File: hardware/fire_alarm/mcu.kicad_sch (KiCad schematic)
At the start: 2 parts, among them U4 ESP32-WROOM-32

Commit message: feat: update power mcu
Signed-off-by: Trung Hieu Nguyen <hieu.nguyenarc03@gmail.com>
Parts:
- added C8: 10uF 25V, Capacitor_SMD:C_0603_1608Metric_Pad1.08x0.95mm_HandSolder, symbol Device:C
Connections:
- net +3.3V: now also C8.2
- net GND: now also C8.1
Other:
- moved on the sheet: C9
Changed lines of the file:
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@@
 	(paper "A4")
 	(junction
-		(at 147.32 50.8)
+		(at 147.32 53.34)
 		(diameter 0)
 		(color 0 0 0 0)
 	)
-	(wire
-		(pts
-			(xy 147.32 50.8) (xy 147.32 63.5)
-		)
-		(stroke
-			(width 0)
-			(type default)
-		)
-	)
-	(wire
-		(pts
-			(xy 135.89 50.8) (xy 132.08 50.8)
-		)
-		(stroke
-			(width 0)
-			(type default)
-		)
-	)
-	(wire
-		(pts
-			(xy 147.32 50.8) (xy 143.51 50.8)
-		)
-		(stroke
-			(width 0)
-			(type default)
-		)
-	)
-	(wire
-		(pts
-			(xy 132.08 50.8) (xy 132.08 57.15)
-		)
-		(stroke
-			(width 0)
-			(type default)
-		)
-	)
-	(wire
-		(pts
-			(xy 147.32 39.37) (xy 147.32 50.8)
+	(junction
+		(at 147.32 45.72)
+		(diameter 0)
+		(color 0 0 0 0)
+	)
+	(junction
+		(at 132.08 53.34)
+		(diameter 0)
+		(color 0 0 0 0)
+	)
+	(wire
+		(pts
+			(xy 132.08 53.34) (xy 135.89 53.34)
+		)
+		(stroke
+			(width 0)
+			(type default)
+		)
+	)
+	(wire
+		(pts
+			(xy 132.08 53.34) (xy 132.08 57.15)
+		)
+		(stroke
+			(width 0)
+			(type default)
+		)
+	)
+	(wire
+		(pts
+			(xy 132.08 45.72) (xy 132.08 53.34)
+		)
+		(stroke
+			(width 0)
+			(type default)
+		)
+	)
+	(wire
+		(pts
+			(xy 147.32 45.72) (xy 147.32 53.34)
+		)
+		(stroke
+			(width 0)
+			(type default)
+		)
+	)
+	(wire
+		(pts
+			(xy 147.32 53.34) (xy 143.51 53.34)
+		)
+		(stroke
+			(width 0)
+			(type default)
+		)
+	)
+	(wire
+		(pts
+			(xy 147.32 39.37) (xy 147.32 45.72)
+		)
+		(stroke
+			(width 0)
+			(type default)
+		)
+	)
+	(wire
+		(pts
+			(xy 147.32 53.34) (xy 147.32 63.5)
 		)
 		(stroke
@@
 		(pts
 			(xy 147.32 134.62) (xy 147.32 144.78)
+		)
+		(stroke
+			(width 0)
+			(type default)
+		)
+	)
+	(wire
+		(pts
+			(xy 135.89 45.72) (xy 132.08 45.72)
+		)
+		(stroke
+			(width 0)
+			(type default)
+		)
+	)
+	(wire
+		(pts
+			(xy 143.51 45.72) (xy 147.32 45.72)
 		)
 		(stroke
@@
 	(symbol
 		(lib_id "Device:C")
-		(at 139.7 50.8 90)
+		(at 139.7 53.34 90)
 		(unit 1)
 		(exclude_from_sim no)
@@
 		(on_board yes)
 		(dnp no)
-		(fields_autoplaced yes)
 		(property "Reference" "C9"
-			(at 139.7 43.18 90)
+			(at 139.446 51.816 90)
 			(effects
 				(font
@@
 		)
 		(property "Value" "100nF 50V"
-			(at 139.7 45.72 90)
+			(at 139.446 54.356 90)
 			(effects
 				(font
@@
 		)
 		(property "Footprint" "Capacitor_SMD:C_0603_1608Metric_Pad1.08x0.95mm_HandSolder"
-			(at 143.51 49.8348 0)
+			(at 143.51 52.3748 0)
 			(effects
 				(font
@@
 		)
 		(property "Datasheet" "~"
-			(at 139.7 50.8 0)
+			(at 139.7 53.34 0)
 			(effects
 				(font
@@
 		)
 		(property "Description" "Unpolarized capacitor"
-			(at 139.7 50.8 0)
+			(at 139.7 53.34 0)
 			(effects
 				(font
@@
 					(unit 1)
 				)
+			)
+		)
+	)
+	(symbol
+		(lib_id "Device:C")
+		(at 139.7 45.72 90)
+		(unit 1)
+		(exclude_from_sim no)
+		(in_bom yes)
+		(on_board yes)
+		(dnp no)
+		(property "Reference" "C8"
+			(at 140.716 44.45 90)
+			(effects
+				(font
+					(size 1.27 1.27)
+				)
+				(justify left)
+			)
+		)
+		(property "Value" "10uF 25V"
+			(at 144.526 46.99 90)
+			(effects
+				(font
+					(size 1.27 1.27)
+				)
+				(justify left)
+			)
+		)
+		(property "Footprint" "Capacitor_SMD:C_0603_1608Metric_Pad1.08x0.95mm_HandSolder"
+			(at 143.51 44.7548 0)
+			(effects
+				(font
+					(size 1.27 1.27)
+				)
+				(hide yes)
+			)
+		)
+		(property "Datasheet" "~"
+			(at 139.7 45.72 0)
+			(effects
+				(font
+					(size 1.27 1.27)
+				)
+				(hide yes)
+			)
+		)
+		(property "Description" "Unpolarized capacitor"
+			(at 139.7 45.72 0)
+			(effects
+				(font
+					(size 1.27 1.27)
+				)
+				(hide yes)
+			)
+		)
+		(pin "1"
+		)
+		(pin "2"
+		)
+		(instances
+			(project "fire_alarm"
+				(path "/0ad2965f-ac4e-45fe-9d64-44da87c25aaa/341ac7be-7be9-46bf-9f34-a87c6324e52b"
+					(reference "C8")
+					(unit 1)
+				)

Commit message: feat: continue laying out schematic MCU
Signed-off-by: Trung Hieu Nguyen <hieu.nguyenarc03@gmail.com>
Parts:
- added C11: 10uF 25V, Capacitor_SMD:C_0603_1608Metric_Pad1.08x0.95mm_HandSolder, symbol Device:C
- added C12: 1uF 16V, Capacitor_SMD:C_0603_1608Metric_Pad1.08x0.95mm_HandSolder, symbol Device:C
- added C13: 100nF 50V, Capacitor_SMD:C_0603_1608Metric_Pad1.08x0.95mm_HandSolder, symbol Device:C
- added J2: USB_C_Receptacle_USB2.0_16P, Connector_USB:USB_C_Receptacle_HRO_TYPE-C-31-M-12, symbol Connector:USB_C_Receptacle_USB2.0_16P
- added R10, R11: 5.1kOhm 0.125W, Resistor_SMD:R_0805_2012Metric_Pad1.20x1.40mm_HandSolder, symbol Device:R
- added R6, R7: 10kOhm 0.1W, Resistor_SMD:R_0201_0603Metric_Pad0.64x0.40mm_HandSolder, symbol Device:R
- added R8, R9: 22Ohm 0.1W, Resistor_SMD:R_0603_1608Metric_Pad0.98x0.95mm_HandSolder, symbol Device:R
- added SW1, SW2: SW_Push, Button_Switch_SMD:SW_Push_SPST_NO_Alps_SKRK, symbol Switch:SW_Push
- added U3: CH340C, Package_SO:SOIC-16_3.9x9.9mm_P1.27mm, symbol Interface_USB:CH340C
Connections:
- net +3.3V: now also C11.2, C13.2, J2.A4 (VBUS), J2.A9 (VBUS), J2.B4 (VBUS), J2.B9 (VBUS), R6.2, R7.2, U3.16 (VCC)
- net GND: now also C11.1, C12.2, C13.1, J2.A1 (GND), J2.A12 (GND), J2.B1 (GND), J2.B12 (GND), R10.1, R11.1, SW1.1, SW2.1, U3.1 (GND)
- net BOOT: now reaches U4.25 (IO0)
- net BOOT: now also R6.1, SW1.2
- net EN: now reaches U4.3 (EN)
- net EN: now also C12.1, R7.1, SW2.2
- new net: R9.2, U3.5 (UD+)
- new net: R8.2, U3.6 (UD-)
- new net: J2.B5 (CC2), R11.2
- new net: J2.A6 (D+), J2.B6 (D+), R9.1
- new net: J2.A5 (CC1), R10.2
- new net: J2.A7 (D-), J2.B7 (D-), R8.1
- no-connect marks 0 -> 9
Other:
- moved on the sheet: C8, C9, U4

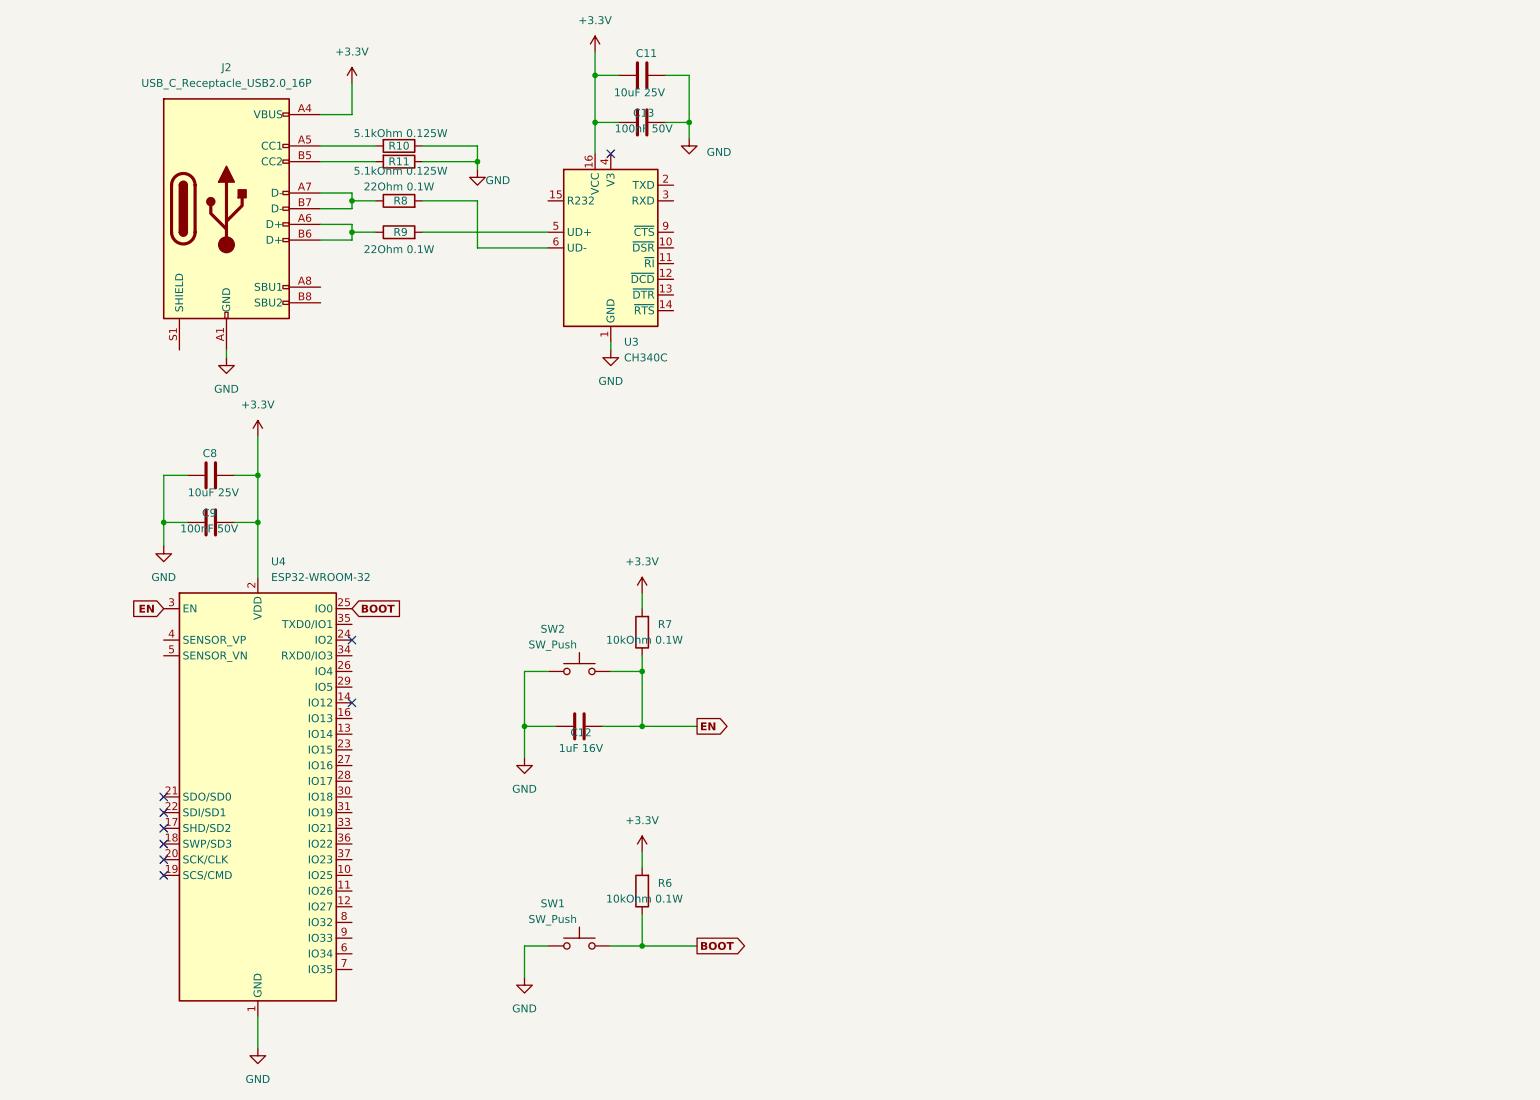
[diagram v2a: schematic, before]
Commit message: feat: update shield pin & v3 pin
Signed-off-by: Trung Hieu Nguyen <hieu.nguyenarc03@gmail.com>
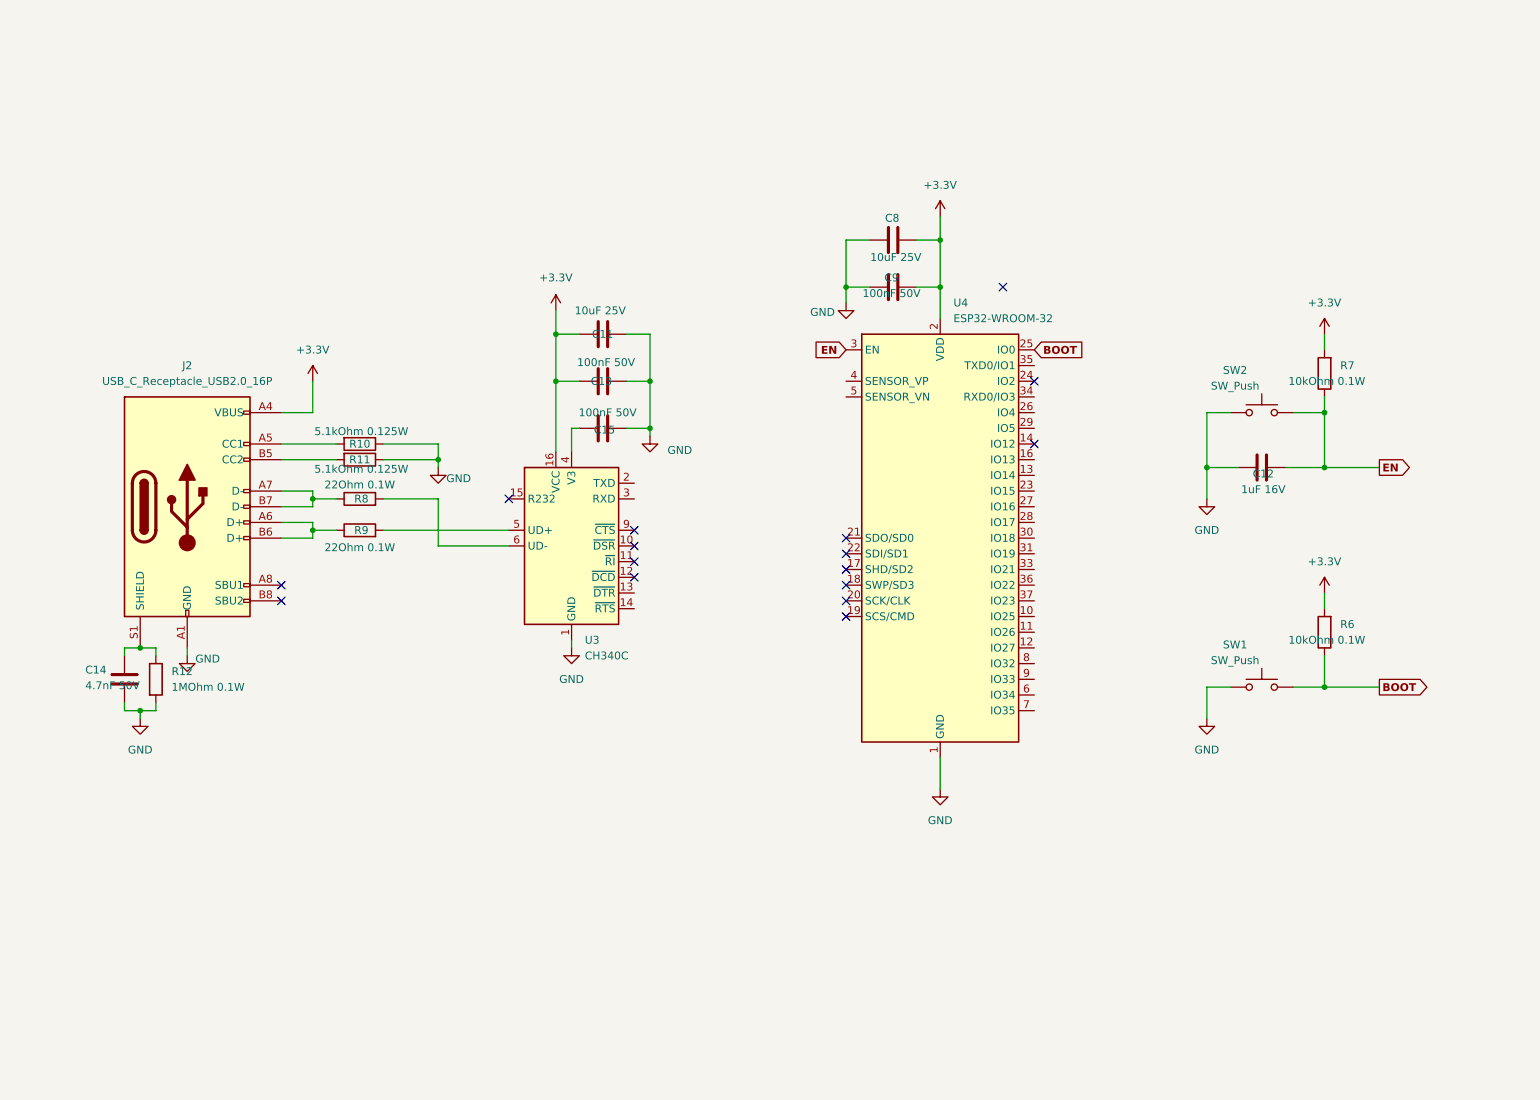
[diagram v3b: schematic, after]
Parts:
- added C14: 4.7nF 50V, Capacitor_SMD:C_0603_1608Metric_Pad1.08x0.95mm_HandSolder, symbol Device:C
- added C15: 100nF 50V, Capacitor_SMD:C_0603_1608Metric_Pad1.08x0.95mm_HandSolder, symbol Device:C
- added R12: 1MOhm 0.1W, Resistor_SMD:R_0603_1608Metric_Pad0.98x0.95mm_HandSolder, symbol Device:R
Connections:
- net GND: now also C14.2, C15.2, R12.2
- net at U3.4 (V3): now also C15.1
- net at J2.S1 (SHIELD): now also C14.1, R12.1
- no-connect marks 9 -> 16
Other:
- moved on the sheet: C11, C12, C13, C8, C9, J2, R10, R11, R6, R7, R8, R9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

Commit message: feat: update schematic sensors, ui
Signed-off-by: Trung Hieu Nguyen <hieu.nguyenarc03@gmail.com>
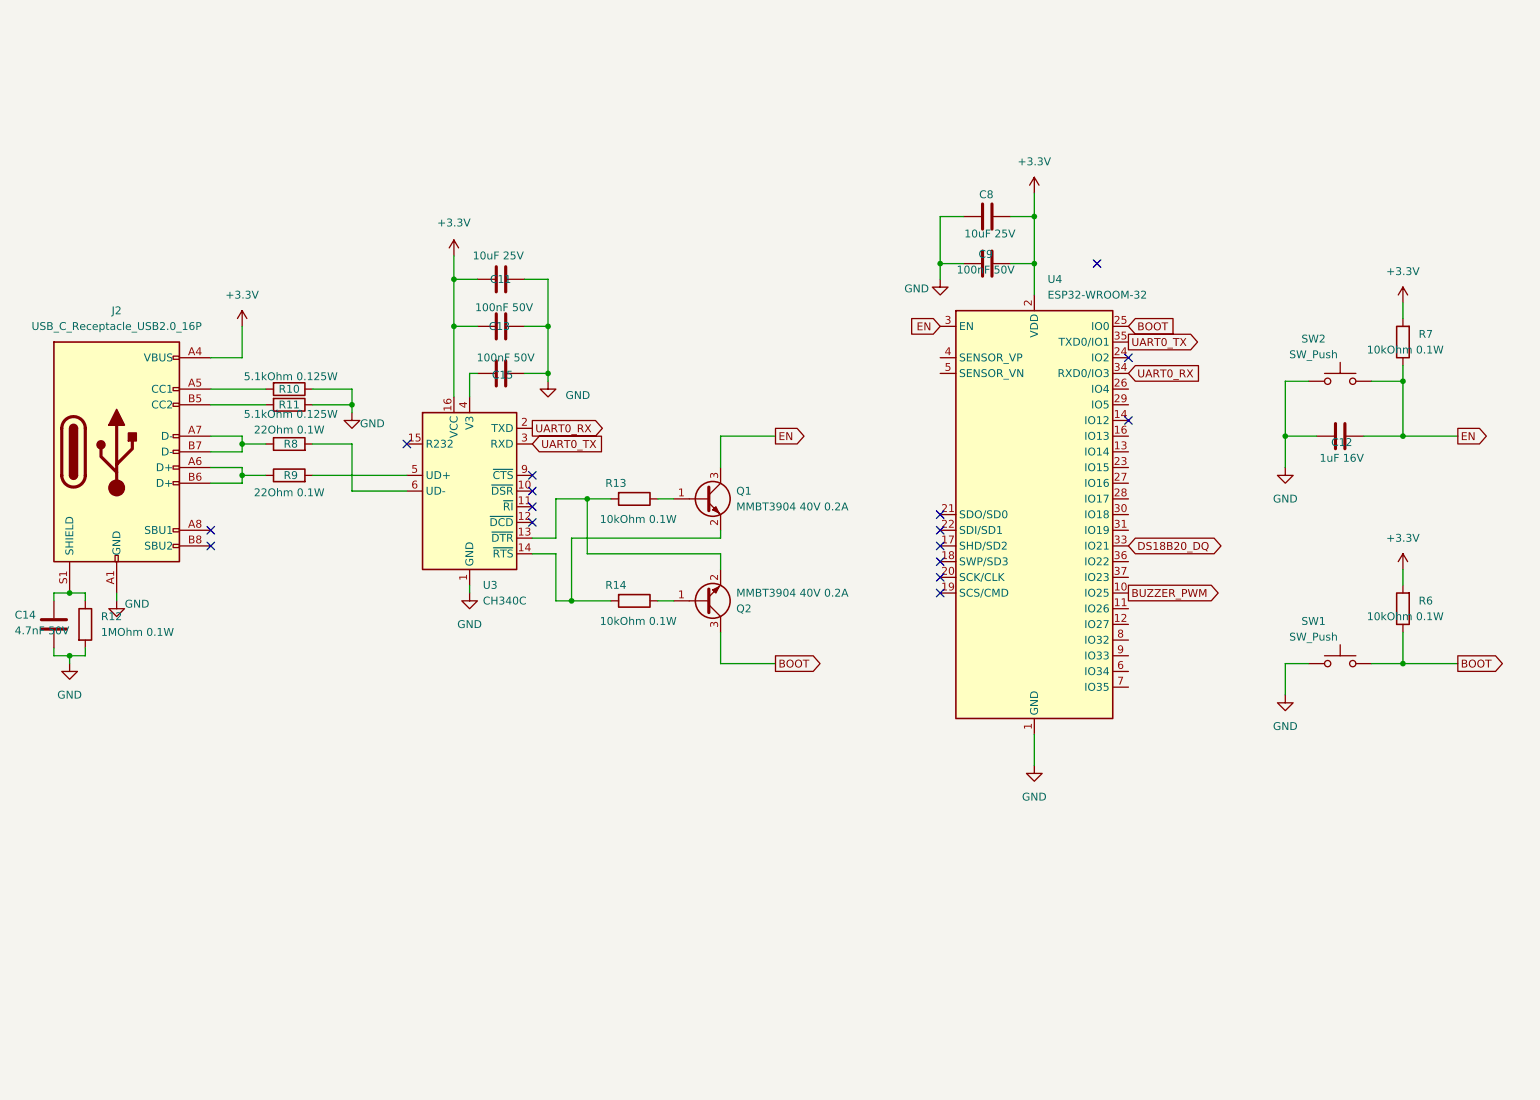
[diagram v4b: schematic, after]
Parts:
- added Q1, Q2: MMBT3904 40V 0.2A, Package_TO_SOT_SMD:SOT-23_Handsoldering, symbol Transistor_BJT:MMBT3904
- added R13, R14: 10kOhm 0.1W, Resistor_SMD:R_0201_0603Metric_Pad0.64x0.40mm_HandSolder, symbol Device:R
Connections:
- net BOOT: now also Q2.3 (C)
- net EN: now also Q1.3 (C)
- net at U3.13 (~{DTR}): now also Q2.2 (E), R13.2
- net at U3.14 (~{RTS}): now also Q1.2 (E), R14.2
- net UART0_RX: now reaches U3.2 (TXD)
- net UART0_RX: now also U4.34 (RXD0/IO3)
- net UART0_TX: now reaches U3.3 (RXD)
- net UART0_TX: now also U4.35 (TXD0/IO1)
- net BUZZER_PWM: now reaches U4.10 (IO25)
- net DS18B20_DQ: now reaches U4.33 (IO21)
- new net: Q1.1 (B), R13.1
- new net: Q2.1 (B), R14.1
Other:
- moved on the sheet: C11, C12, C13, C14, C15, C8, C9, J2, R10, R11, R12, R6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

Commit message: feat: complete schematic
Signed-off-by: Trung Hieu Nguyen <hieu.nguyenarc03@gmail.com>
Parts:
- added D4: LED GREEN, LED_SMD:LED_0805_2012Metric_Pad1.15x1.40mm_HandSolder, symbol Device:LED
- added R18: 33Ohm 0.1W, Resistor_SMD:R_0603_1608Metric_Pad0.98x0.95mm_HandSolder, symbol Device:R
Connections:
- net GND: now also D4.1 (K)
- net MAX30105_INT: now reaches U4.11 (IO26)
- net I2C_SDA: now reaches U4.30 (IO18)
- net I2C_SCL: now reaches U4.31 (IO19)
- net LED_DEBUG: now reaches U4.36 (IO22)
- net LED_DEBUG: now also R18.1
- net LED_ALARM: now reaches U4.37 (IO23)
- new net: D4.2 (A), R18.2
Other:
- moved on the sheet: C12, R6, R7, SW1, SW2
